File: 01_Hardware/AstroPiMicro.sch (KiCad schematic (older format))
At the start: 40 parts, among them J1 RPi Connector, J10 6-pin JST PH, J2 USB_C_Receptacle_USB2.0, J3 2-pin JST PH, J4 4-pin JST SH, J5 4-pin JST SH, J6 11-pin JST PH, J7 3-pin JST PH, J8 3-pin JST PH, J9 6-pin JST PH, SW1 SW-ON-OFF, U1 LM809, U2 STM32G431KBTx, U3 MCP73831-2-OT, U4 TPS61090, U5 Joystick, Y1 16MHz

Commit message: Started on HW version 2
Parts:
- removed C6: 100nF, Capacitor_SMD:C_0603_1608Metric_Pad1.05x0.95mm_HandSolder, symbol Device:C_Small
- removed D1: Status LED, LED_SMD:LED_Avago_PLCC4_3.2x2.8mm_CW, symbol Device:LED_Dual_CACA
- removed J10: 6-pin JST PH, Connector_JST:JST_PH_B6B-PH-K_1x06_P2.00mm_Vertical, symbol Connector_Generic:Conn_01x06
- removed J2: USB_C_Receptacle_USB2.0, astropi:USB_C_GCT_USB4085, symbol Connector:USB_C_Receptacle_USB2.0
- removed J6: 11-pin JST PH, Connector_JST:JST_PH_B11B-PH-K_1x11_P2.00mm_Vertical, symbol Connector_Generic:Conn_01x11
- removed J7: 3-pin JST PH, Connector_JST:JST_PH_B3B-PH-K_1x03_P2.00mm_Vertical, symbol Connector_Generic:Conn_01x03
- removed J8: 3-pin JST PH, Connector_JST:JST_PH_B3B-PH-SM4-TB_1x03-1MP_P2.00mm_Vertical, symbol Connector_Generic:Conn_01x03
- removed J9: 6-pin JST PH, Connector_JST:JST_PH_B6B-PH-SM4-TB_1x06-1MP_P2.00mm_Vertical, symbol Connector_Generic:Conn_01x06
- removed U1: LM809, Package_TO_SOT_SMD:SOT-23, symbol Power_Supervisor:LM809
- removed U2: STM32G431KBTx, Package_QFP:LQFP-32_7x7mm_P0.8mm, symbol MCU_ST_STM32G4:STM32G431KBTx
- removed U3: MCP73831-2-OT, Package_TO_SOT_SMD:SOT-23-5, symbol Battery_Management:MCP73831-2-OT
- removed U5: Joystick, astropi:SKRHAAE010, symbol joystick:SKRHAAE010
- removed Y1: 16MHz, Crystal:Crystal_SMD_Abracon_ABM3B-4Pin_5.0x3.2mm, symbol Device:Crystal_GND24_Small
- added C11, C12, C14, C15, C16, C18: 100nF, Capacitor_SMD:C_0603_1608Metric, symbol Device:C_Small
- added C13, C17, C6: 47uF, Capacitor_Tantalum_SMD:CP_EIA-3528-15_AVX-H, symbol Device:CP_Small
- added C3: 4.7uF, Capacitor_SMD:C_0805_2012Metric, symbol Device:C_Small
- added D1: Green, LED_SMD:LED_0603_1608Metric, symbol Device:LED_Small
- added D2: Orange, LED_SMD:LED_0603_1608Metric, symbol Device:LED_Small
- added J2: SHOU_HAN_TYPE-C_6P, astropi:SHOU HAN TYPE-C 6P, symbol astropi:SHOU_HAN_TYPE-C_6P
- added J6: Stepper_Azimuth, Connector_JST:JST_XH_S4B-XH-A_1x04_P2.50mm_Horizontal, symbol Connector_Generic:Conn_01x04
- added J7: Stepper_Altitude, Connector_JST:JST_XH_S4B-XH-A_1x04_P2.50mm_Horizontal, symbol Connector_Generic:Conn_01x04
- added R11, R14: 0.75, Resistor_SMD:R_0603_1608Metric, symbol Device:R_Small
- added R15, R18: 1k, Resistor_SMD:R_0603_1608Metric, symbol Device:R_Small
- added R16, R17, R19, R20: 220m, Resistor_SMD:R_0603_1608Metric, symbol Device:R_Small
- added R21: 10k, Resistor_SMD:R_0603_1608Metric, symbol Device:R_Small
- added TP1: TP_VBAT, TestPoint:TestPoint_Pad_D2.0mm, symbol Connector:TestPoint
- added TP2: TP_Supply, TestPoint:TestPoint_Pad_D2.0mm, symbol Connector:TestPoint
- added TP3: TP_5V, TestPoint:TestPoint_Pad_D2.0mm, symbol Connector:TestPoint
- added TP4: TP_GND, TestPoint:TestPoint_Pad_2.5x2.5mm, symbol Connector:TestPoint
- added U1: BQ24074RGT, Package_DFN_QFN:VQFN-16-1EP_3x3mm_P0.5mm_EP1.6x1.6mm_ThermalVias, symbol Battery_Management:BQ24074RGT
- added U2, U3, U5: TMC2300, Package_DFN_QFN:QFN-20-1EP_3x3mm_P0.4mm_EP1.65x1.65mm_ThermalVias, symbol astropi:TMC2300
- C1: value 27pF -> 100nF; footprint Capacitor_SMD:C_0603_1608Metric_Pad1.05x0.95mm_HandSolder -> Capacitor_SMD:C_0603_1608Metric; LCSC (none) -> C187860; MPN GRM1885C1H270JA01D -> C0603X104K050T
- C10: footprint Capacitor_Tantalum_SMD:CP_EIA-7343-31_Kemet-D_Pad2.25x2.55mm_HandSolder -> Capacitor_Tantalum_SMD:CP_EIA-7343-15_Kemet-W; LCSC (none) -> C122321
- C2: value 27pF -> 1uF; footprint Capacitor_SMD:C_0603_1608Metric_Pad1.05x0.95mm_HandSolder -> Capacitor_SMD:C_0805_2012Metric; LCSC (none) -> C116352; MPN GRM1885C1H270JA01D -> CL21B105KAFNNNE
- C4: value 100nF -> 10uF; footprint Capacitor_SMD:C_0603_1608Metric_Pad1.05x0.95mm_HandSolder -> Capacitor_SMD:C_0805_2012Metric; LCSC (none) -> C40894; MPN 0603B104K500AT -> 0805X106K250NT
- C5: value 10uF -> 100nF; footprint Capacitor_SMD:C_0805_2012Metric -> Capacitor_SMD:C_0603_1608Metric; LCSC (none) -> C187860; MPN C2012X5R1C106KTJ00E -> C0603X104K050T
- C7: footprint Capacitor_SMD:C_0603_1608Metric_Pad1.05x0.95mm_HandSolder -> Capacitor_SMD:C_0603_1608Metric; LCSC (none) -> C187860; MPN 0603B104K500AT -> C0603X104K050T
- C8: LCSC (none) -> C40894; MPN C2012X5R1C106KTJ00E -> 0805X106K250NT
- C9: LCSC (none) -> C106842
- J3: LCSC (none) -> C47647
- J4: LCSC (none) -> C145956
- J5: value 4-pin JST SH -> Stepper_Focus; footprint Connector_JST:JST_SH_BM04B-SRSS-TB_1x04-1MP_P1.00mm_Vertical -> Connector_JST:JST_XH_S4B-XH-A_1x04_P2.50mm_Horizontal; LCSC (none) -> C157925; MPN A1002WV-S-4P -> S4B-XH-A(LF)(SN)
- L1: value 6.8uH -> 10uH; footprint Inductor_SMD:L_Taiyo-Yuden_NR-50xx_HandSoldering -> astropi:VLS6045EX-100M; LCSC (none) -> C360734; MPN NRS5040T6R8MMGJ -> VLS6045EX-100M
- R1: value 10k -> 1.1k; footprint Resistor_SMD:R_0603_1608Metric_Pad1.05x0.95mm_HandSolder -> Resistor_SMD:R_0603_1608Metric; LCSC (none) -> C22764; MPN 0603WAJ0103T5E -> 0603WAF1101T5E
- R10: footprint Resistor_SMD:R_0603_1608Metric_Pad1.05x0.95mm_HandSolder -> Resistor_SMD:R_0603_1608Metric; LCSC (none) -> C307295
- R12: footprint Resistor_SMD:R_0603_1608Metric_Pad1.05x0.95mm_HandSolder -> Resistor_SMD:R_0603_1608Metric; LCSC (none) -> C61679
- R13: footprint Resistor_SMD:R_0603_1608Metric_Pad1.05x0.95mm_HandSolder -> Resistor_SMD:R_0603_1608Metric; LCSC (none) -> C22949
- R2: value 10k -> 1k; footprint Resistor_SMD:R_0603_1608Metric_Pad1.05x0.95mm_HandSolder -> Resistor_SMD:R_0603_1608Metric; LCSC (none) -> C101253; MPN 0603WAJ0103T5E -> CR0603JA0102G
- R3: value 10k -> 1.5k; footprint Resistor_SMD:R_0603_1608Metric_Pad1.05x0.95mm_HandSolder -> Resistor_SMD:R_0603_1608Metric; LCSC (none) -> C114680; MPN 0603WAJ0103T5E -> RC0603JR-071K5L
- R4, R5: footprint Resistor_SMD:R_0603_1608Metric_Pad1.05x0.95mm_HandSolder -> Resistor_SMD:R_0603_1608Metric; LCSC (none) -> C23186
- R6: value 2k -> 10k; footprint Resistor_SMD:R_0603_1608Metric_Pad1.05x0.95mm_HandSolder -> Resistor_SMD:R_0603_1608Metric; LCSC (none) -> C99198; MPN CR0603FA2001G -> RC0603JR-0710KL
- R7, R8: footprint Resistor_SMD:R_0603_1608Metric_Pad1.05x0.95mm_HandSolder -> Resistor_SMD:R_0603_1608Metric; LCSC (none) -> C101253; MPN 0603WAF1001T5E -> CR0603JA0102G
- R9: footprint Resistor_SMD:R_0603_1608Metric_Pad1.05x0.95mm_HandSolder -> Resistor_SMD:R_0603_1608Metric; LCSC (none) -> C166860
- SW1: value SW-ON-OFF -> SW_SPDT; footprint astropi:SSSS213202 -> Button_Switch_SMD:SW_SPDT_CK-JS102011SAQN; LCSC (none) -> C221660; MPN SSSS213202 -> JS102011SAQN
- U4: value TPS61090 -> TPS61030; LCSC (none) -> C10110; MPN TPS61090RSAR -> TPS61030RSAR
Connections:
- net SW_1 is gone; now on net GND: SW1.1 (A)
- net SW_2 is gone; now on net ON\~OFF: SW1.2 (B)
- net +3V3: now also C1.1, C11.1, C15.1, U2.11 (VIO/~STDBY), U2.7 (EN), U2.8 (STEPPER), U3.11 (VIO/~STDBY), U3.5 (MS1/AD0), U3.7 (EN), U3.8 (STEPPER), U5.11 (VIO/~STDBY), U5.5 (MS1/AD0), U5.6 (MS2/AD1), U5.7 (EN), U5.8 (STEPPER); no longer C4.1, C7.1, J5.1 (Pin_1), R1.1, R3.1
- net +5V: now also C5.1, C12.1, C13.1, C16.1, C17.1, C6.1, TP3.1, U2.18 (VS), U3.18 (VS), U5.18 (VS)
- net +BATT: now also C3.1, TP1.1, U1.2 (BAT), U1.3 (BAT); no longer C8.1, L1.1, R9.1, U4.8 (VBAT)
- net GND: now also R1.1, R3.1, C11.2, C12.2, C13.2, C14.2, C15.2, C16.2, C17.2, C18.2, C3.2, C6.2, J2.A12 (GND), J2.B12 (GND), J2.S1 (SHIELD), R11.2, R14.2, R16.2, R17.2, R19.2, R20.2, TP4.1, U1.14 (TMR), U1.17 (VSS), U1.4 (~CE), U1.6 (EN1), U1.8 (VSS), U2.14 (GND), U2.21 (PAD), U2.5 (MS1/AD0), U2.6 (MS2/AD1), U2.9 (MODE), U3.14 (GND), U3.21 (PAD), U3.6 (MS2/AD1), U3.9 (MODE), U5.14 (GND), U5.21 (PAD), U5.9 (MODE); no longer J5.4 (Pin_4), R2.2, R8.2
- net IMU_SCL: now also J1.5 (Pin_5)
- net IMU_SDA: now also J1.3 (Pin_3)
- net ON\~OFF: now also R21.2
- net VBUS: now also C2.1, J2.A9 (VBUS), J2.B9 (VBUS), U1.13 (IN); no longer C5.1
- net STEP_Alt: now reaches J1.29 (Pin_29)
- net STEP_Alt: now also U5.4 (STEP)
- net DIR_Alt: now reaches J1.31 (Pin_31)
- net DIR_Alt: now also U5.3 (DIR)
- net ERR_Alt: now reaches J1.33 (Pin_33)
- net ERR_Alt: now also U5.12 (DIAG)
- net at R4.2: now also J2.A5 (CC1)
- net at R5.2: now also J2.B5 (CC2)
- net Vsupply: now reaches R7.1
- net Vsupply: now also C4.1, C8.1, L1.1, R8.1, R9.1, U4.8 (VBAT), R21.1, TP2.1, U1.10 (OUT), U1.11 (OUT), U1.5 (EN2)
- net at R6.1: now also U1.1 (TS)
- net at R3.2: now also U1.16 (ISET); no longer R2.1
- net CHG_ST: no longer names the net of R7.2
- net CHG_ST: now also D1.2 (A)
- net GPIO17 renamed STEP_Focus
- net STEP_Focus: now also U2.4 (STEP)
- net GPIO22 renamed ERR_Focus
- net ERR_Focus: now also U2.12 (DIAG)
- net GPIO23: no longer names the net of J1.16 (Pin_16)
- net GPIO27 renamed DIR_Focus
- net DIR_Focus: now also U2.3 (DIR)
- net GPIO4: no longer names the net of J1.7 (Pin_7)
- net LCD_BL: no longer names the net of J1.35 (Pin_35)
- net LCD_MOSI renamed STEP_Az
- net STEP_Az: now also U3.4 (STEP)
- net LCD_SCK renamed ERR_Az
- net ERR_Az: now also U3.12 (DIAG)
- net LCD_TDC renamed DIR_Az
- net DIR_Az: now also U3.3 (DIR)
- net LCD_~TCS: no longer names the net of J1.26 (Pin_26)
- net PI_UART_RX renamed UART_RX
- net UART_RX: now also R2.2, R15.2, R18.2, U2.10 (UART), U3.10 (UART), U5.10 (UART)
- net PI_UART_TX renamed UART_TX
- net UART_TX: now also R2.1, R15.1, R18.1
- net SWCLK renamed Focus_B1
- net Focus_B1: now also U2.17 (OB1)
- net SWDIO renamed Focus_A2
- net Focus_A2: now also U2.1 (OA2)
- net SW_3: no longer names the net of SW1.3 (C)
- net ~RESET: no longer names the net of R1.2
- net ~RESET: now also U1.12 (ILIM)
- new net: C7.1, U2.13 (1V8)
- new net: R11.1, U2.16 (BRB)
- new net: R14.1, U2.20 (BRA)
- new net: C14.1, U3.13 (1V8)
- new net: R16.1, U3.16 (BRB)
- new net: R17.1, U3.20 (BRA)
- new net: C18.1, U5.13 (1V8)
- new net: R19.1, U5.16 (BRB)
- new net: R20.1, U5.20 (BRA)
- new net: D1.1 (K), U1.7 (~PGOOD)
- new net: D2.1 (K), U1.9 (~CHG)
- new net: D2.2 (A), R8.2
- new net Alt_A1: J7.1 (Pin_1), U5.19 (OA1)
- new net Alt_A2: J7.2 (Pin_2), U5.1 (OA2)
- new net Alt_B1: J7.3 (Pin_3), U5.17 (OB1)
- new net Alt_B2: J7.4 (Pin_4), U5.15 (OB2)
- new net Az_A1: J6.1 (Pin_1), U3.19 (OA1)
- new net Az_A2: J6.2 (Pin_2), U3.1 (OA2)
- new net Az_B1: J6.3 (Pin_3), U3.17 (OB1)
- new net Az_B2: J6.4 (Pin_4), U3.15 (OB2)
- new net Focus_A1: J5.1 (Pin_1), U2.19 (OA1)
- new net Focus_B2: J5.4 (Pin_4), U2.15 (OB2)
- no-connect marks 41 -> 19
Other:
- note added: "- ~LOW_BAT~ should have internal pull-up!"
- note added: "1.5A current limit\n600mA charge current"
- note added: "290mA"
- note added: "870mA"
- note added: "Address\nConfiguration"
- note added: "Charger and USB power manager"
- note added: "JST XH"
- note added: "USB PMIC & Charging"
- note removed: "- All Joystick GPIOs & ~LOW_BAT~ have internal pull-up resistors!"
- note removed: "500mA charge current"
- note removed: "G"
- note removed: "Joystick"
- note removed: "Non-shorting / Break before make"
- note removed: "ON/OFF Switch"
- note removed: "QWIIC (V)\nConnector"
- note removed: "Reset circuit"
- note removed: "USB + Charging"
- note removed: "Y"
- note removed: "uC"
- moved on the sheet: C10, C8, C9, J1, J3, J4, L1, R10, R12, R13, R4, R5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

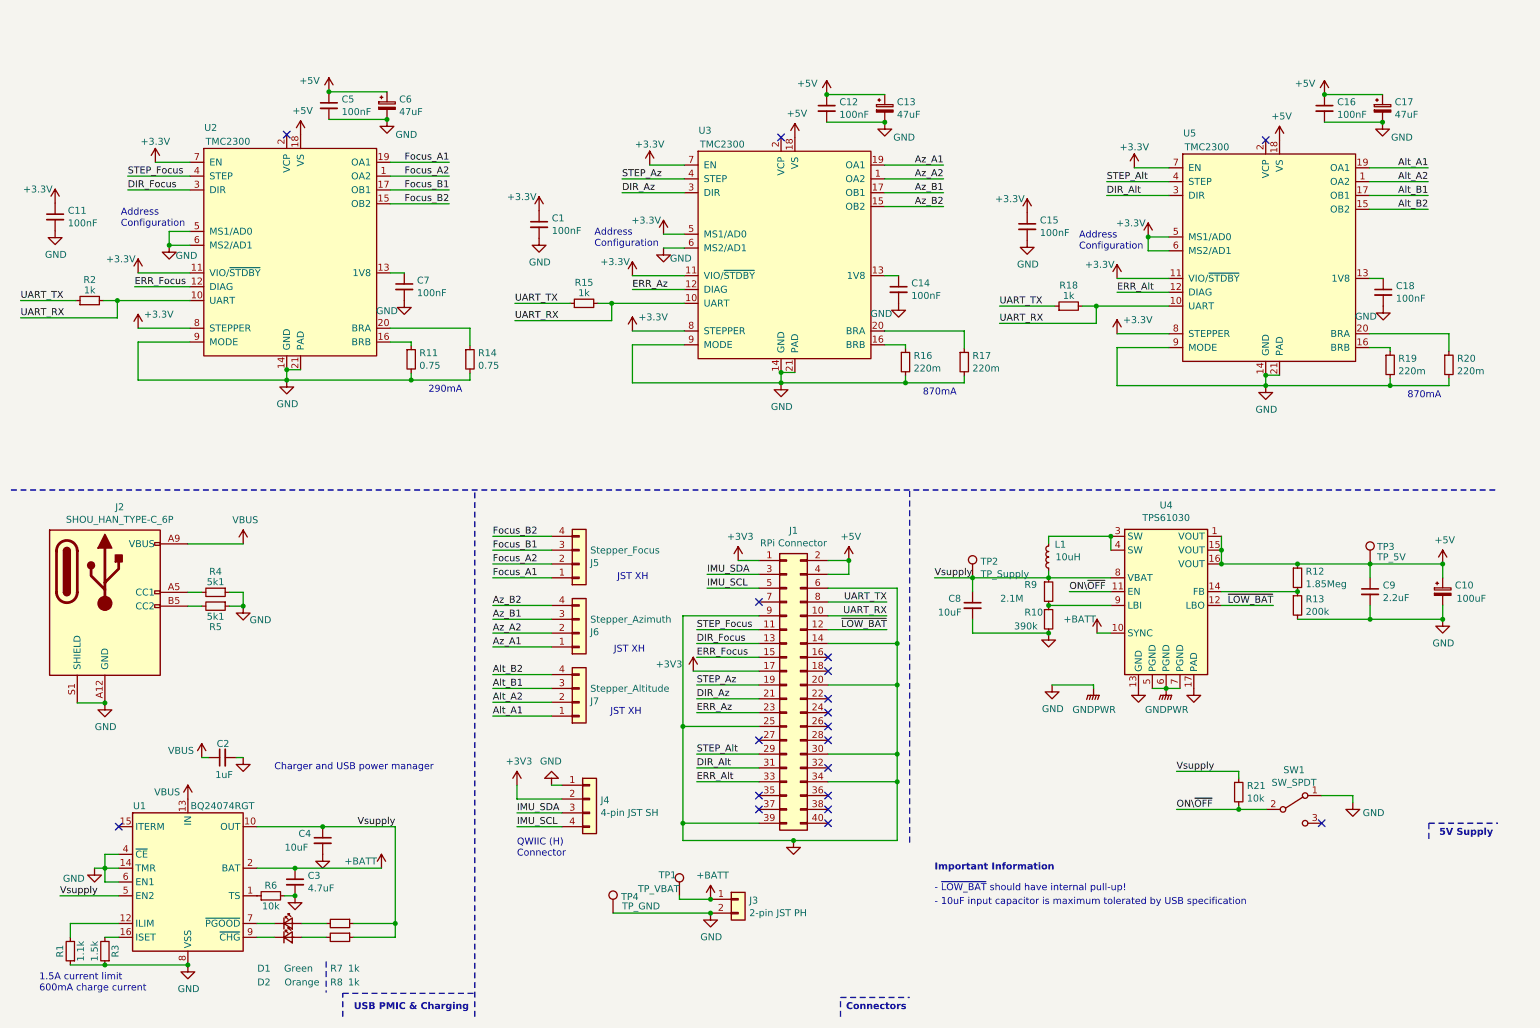
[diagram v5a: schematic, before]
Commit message: Ordered PCBs from JLCPCB
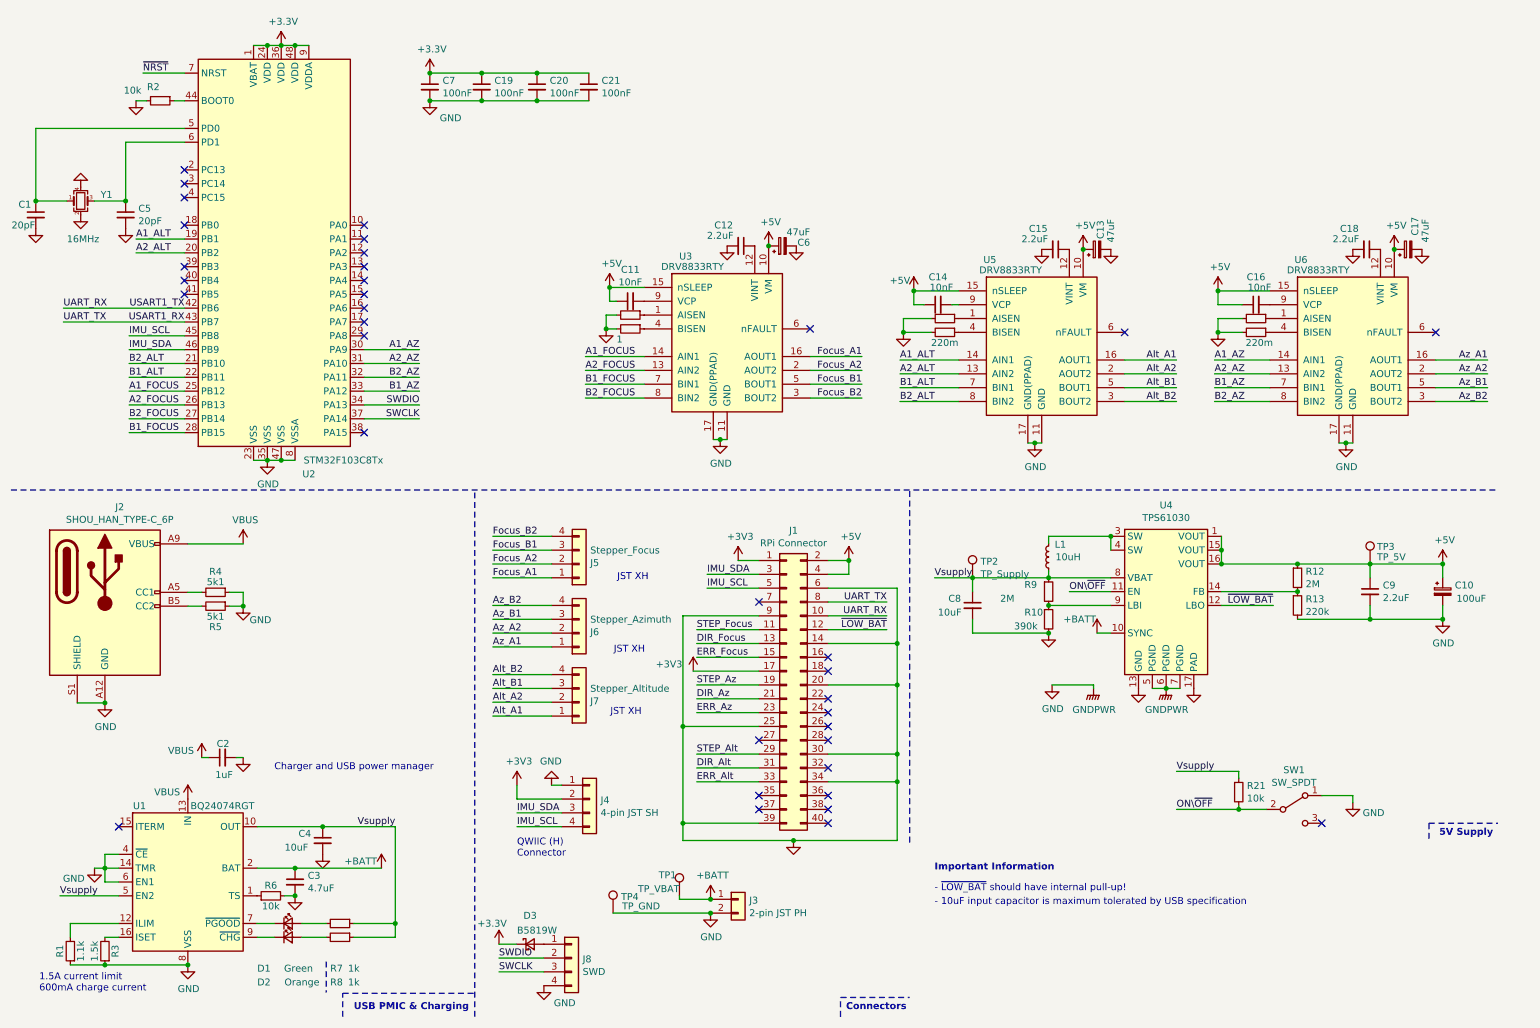
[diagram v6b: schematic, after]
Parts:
- removed R15, R18: 1k, Resistor_SMD:R_0603_1608Metric, symbol Device:R_Small
- removed U2, U3, U5: TMC2300, Package_DFN_QFN:QFN-20-1EP_3x3mm_P0.4mm_EP1.65x1.65mm_ThermalVias, symbol astropi:TMC2300
- added C19, C20, C21: 100nF, Capacitor_SMD:C_0603_1608Metric, symbol Device:C_Small
- added D3: B5819W, Diode_SMD:D_SOD-123, symbol Device:D_Schottky_Small
- added J8: SWD, Connector_JST:JST_SH_BM04B-SRSS-TB_1x04-1MP_P1.00mm_Vertical, symbol Connector_Generic:Conn_01x04
- added U2: STM32F103C8Tx, Package_QFP:LQFP-48_7x7mm_P0.5mm, symbol MCU_ST_STM32F1:STM32F103C8Tx
- added U3, U5, U6: DRV8833RTY, Package_DFN_QFN:Texas_S-PWQFN-N16_EP2.1x2.1mm_ThermalVias, symbol Driver_Motor:DRV8833RTY
- added Y1: 16MHz, Crystal:Crystal_SMD_3225-4Pin_3.2x2.5mm, symbol Device:Crystal_GND24_Small
- C1, C5: value 100nF -> 20pF; LCSC C187860 -> C1648; MPN C0603X104K050T -> (none)
- C11, C14, C16: value 100nF -> 10nF; LCSC C187860 -> C57112; MPN C0603X104K050T -> (none)
- C12, C15, C18: value 100nF -> 2.2uF; footprint Capacitor_SMD:C_0603_1608Metric -> Capacitor_SMD:C_0805_2012Metric; LCSC C187860 -> C49217; MPN C0603X104K050T -> (none)
- C2: LCSC C116352 -> C28323
- C3: LCSC C92762 -> C1779
- C7: LCSC C187860 -> C14663; MPN C0603X104K050T -> (none)
- C9: LCSC C106842 -> C49217
- L1: footprint astropi:VLS6045EX-100M -> Inductor_SMD:L_Sunlord_MWSA0518_5.4x5.2mm; LCSC C360734 -> C139506
- R10: LCSC C307295 -> C23150
- R11, R14: value 0.75 -> 1; footprint Resistor_SMD:R_0603_1608Metric -> Resistor_SMD:R_1206_3216Metric; LCSC C158878 -> C17928; MPN RTT03R75JTP -> (none)
- R12: value 1.85Meg -> 2M; LCSC C61679 -> C22976
- R13: value 200k -> 220k; LCSC C22949 -> C22961
- R16, R17, R19, R20: footprint Resistor_SMD:R_0603_1608Metric -> Resistor_SMD:R_1206_3216Metric; LCSC C20686 -> C25336; MPN 0603WAF220LT5E -> (none)
- R2: value 1k -> 10k; LCSC C101253 -> C25804; MPN CR0603JA0102G -> (none)
- R21, R6: LCSC C99198 -> C25804
- R3: LCSC C114680 -> C22843
- R7, R8: LCSC C101253 -> C21190
- R9: value 2.1M -> 2M; LCSC C166860 -> C22976
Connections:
- net +3V3: now also C7.1, C19.1, C20.1, C21.1, D3.1 (K), U2.1 (VBAT), U2.24 (VDD), U2.36 (VDD), U2.48 (VDD), U2.9 (VDDA); no longer C1.1, C11.1, C15.1
- net +5V: now also C11.1, C14.1, U3.10 (VM), U3.15 (nSLEEP), U5.10 (VM), U5.15 (nSLEEP), U6.10 (VM), U6.15 (nSLEEP); no longer C12.1, C5.1
- net Alt_A1: now also U5.16 (AOUT1)
- net Alt_A2: now also U5.2 (AOUT2)
- net Alt_B1: now also U5.5 (BOUT1)
- net Alt_B2: now also U5.3 (BOUT2)
- net Az_A1: now also U6.16 (AOUT1)
- net Az_A2: now also U6.2 (AOUT2)
- net Az_B1: now also U6.5 (BOUT1)
- net Az_B2: now also U6.3 (BOUT2)
- net Focus_A1: now also U3.16 (AOUT1)
- net Focus_A2: now also U3.2 (AOUT2)
- net Focus_B1: now also U3.5 (BOUT1)
- net Focus_B2: now also U3.3 (BOUT2)
- net GND: now also R2.2, C19.2, C20.2, C21.2, J8.4 (Pin_4), U2.23 (VSS), U2.35 (VSS), U2.47 (VSS), U2.8 (VSSA), U3.11 (GND), U3.17 (GND(PPAD)), U5.11 (GND), U5.17 (GND(PPAD)), U6.11 (GND), U6.17 (GND(PPAD)), Y1.2, Y1.4; no longer C11.2, C14.2, C16.2
- net IMU_SCL: now also U2.45 (PB8)
- net IMU_SDA: now also U2.46 (PB9)
- net UART_RX: now also U2.42 (PB6); no longer R2.2
- net UART_TX: now also U2.43 (PB7); no longer R2.1
- net at R11.1: now also U3.1 (AISEN)
- net at R14.1: now also U3.4 (BISEN)
- net at R16.1: now also U5.1 (AISEN)
- net at R17.1: now also U5.4 (BISEN)
- net at C18.1: now also U6.12 (VINT)
- net at R19.1: now also U6.4 (BISEN)
- net at R20.1: now also U6.1 (AISEN)
- new net: C12.1, U3.12 (VINT)
- new net: C11.2, U3.9 (VCP)
- new net: R2.1, U2.44 (BOOT0)
- new net: C1.1, U2.5 (PD0), Y1.1
- new net: C5.1, U2.6 (PD1), Y1.3
- new net: C15.1, U5.12 (VINT)
- new net: C14.2, U5.9 (VCP)
- new net: C16.2, U6.9 (VCP)
- new net: D3.2 (A), J8.1 (Pin_1)
- new net A1_ALT: U2.19 (PB1), U5.14 (AIN1)
- new net A1_AZ: U2.30 (PA9), U6.14 (AIN1)
- new net A1_FOCUS: U2.25 (PB12), U3.14 (AIN1)
- new net A2_ALT: U2.20 (PB2), U5.13 (AIN2)
- new net A2_AZ: U2.31 (PA10), U6.13 (AIN2)
- new net A2_FOCUS: U2.26 (PB13), U3.13 (AIN2)
- new net B1_ALT: U2.22 (PB11), U5.7 (BIN1)
- new net B1_AZ: U2.33 (PA12), U6.7 (BIN1)
- new net B1_FOCUS: U2.28 (PB15), U3.7 (BIN1)
- new net B2_ALT: U2.21 (PB10), U5.8 (BIN2)
- new net B2_AZ: U2.32 (PA11), U6.8 (BIN2)
- new net B2_FOCUS: U2.27 (PB14), U3.8 (BIN2)
- new net SWCLK: J8.3 (Pin_3), U2.37 (PA14)
- new net SWDIO: J8.2 (Pin_2), U2.34 (PA13)
- new net ~NRST: U2.7 (NRST)
- no-connect marks 19 -> 36
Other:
- note removed: "290mA"
- note removed: "870mA"
- note removed: "Address\nConfiguration"
- moved on the sheet: C13, C17, C6

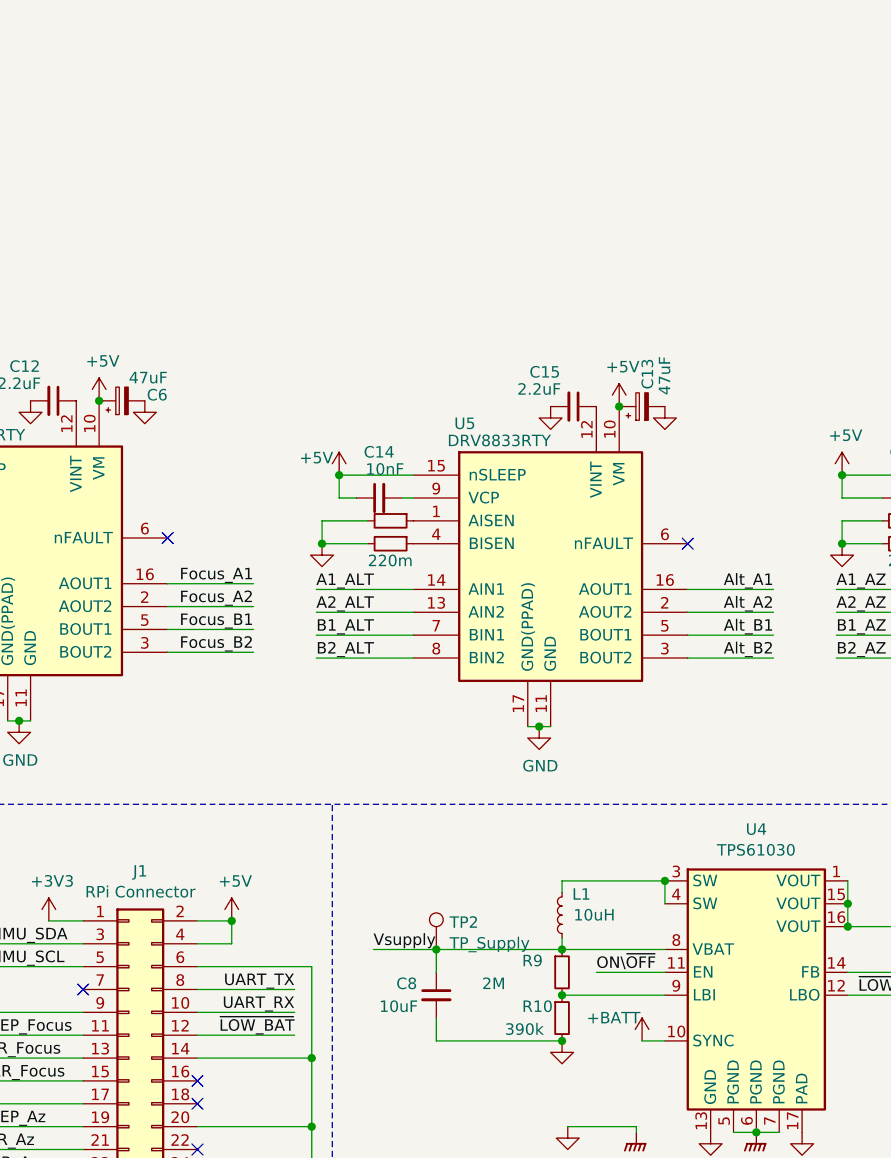
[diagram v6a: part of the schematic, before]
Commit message: Changed layers to Sig, GND, PWR, Sig
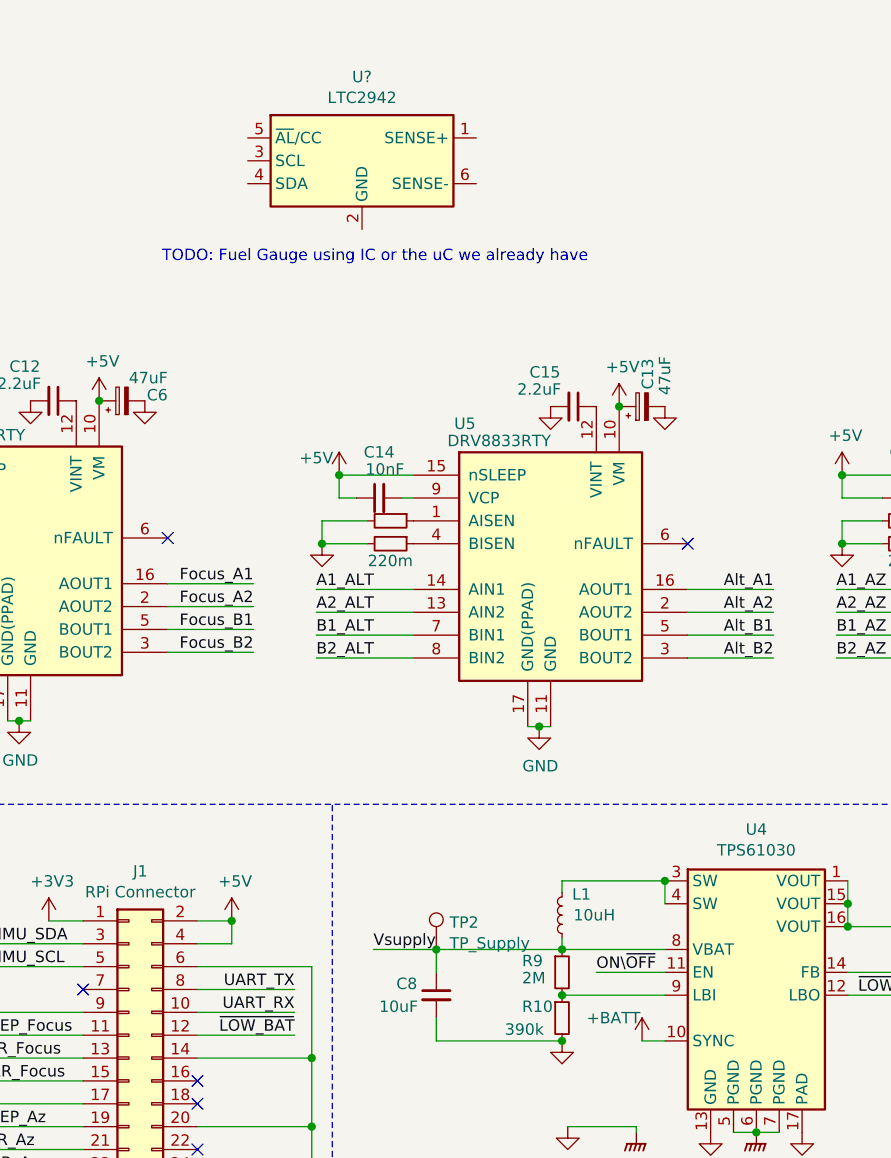
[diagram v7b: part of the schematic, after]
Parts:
- added U?: LTC2942, Package_DFN_QFN:DFN-6-1EP_3x2mm_P0.5mm_EP1.65x1.35mm, symbol Battery_Management:LTC2942
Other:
- note added: "TODO: Fuel Gauge using IC or the uC we already have"
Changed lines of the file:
@@
 AR Path="/5EB652FF" Ref="R9"  Part="1"
 F 0 "R9" H 7800 4775 50  0000 L CNN
-F 1 "2M" H 7625 4675 50  0000 L CNN
+F 1 "2M" H 7800 4700 50  0000 L CNN
 F 2 "Resistor_SMD:R_0603_1608Metric" H 7975 4725 50  0001 C CNN
 F 3 "~" H 7975 4725 50  0001 C CNN
@@
 Wire Wire Line
 	4000 7275 4125 7275
+$Comp
+L Battery_Management:LTC2942 U?
+U 1 1 5F193E19
+P 7100 1175
+F 0 "U?" H 7100 1542 50  0000 C CNN
+F 1 "LTC2942" H 7100 1451 50  0000 C CNN
+F 2 "Package_DFN_QFN:DFN-6-1EP_3x2mm_P0.5mm_EP1.65x1.35mm" H 7100 1525 50  0001 C CNN
+F 3 "https://www.analog.com/media/en/technical-documentation/data-sheets/2942fa.pdf" H 7100 1125 50  0001 C CNN
+	1    7100 1175
+	1    0    0    -1
+$EndComp
+Text Notes 6225 1625 0    50   ~ 0
+TODO: Fuel Gauge using IC or the uC we already have
 $EndSCHEMATC
